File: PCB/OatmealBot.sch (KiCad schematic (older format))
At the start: 23 parts, among them J1 TerminalBlock_5pin_3.5mm, J10 ServoHeader3, J2 RPi_GPIO, J3 TerminalBlock_5pin_3.5mm, J4 ServoHeader1, J5 Motor 3, J6 Motor 4, J7 ServoHeader2, J8 Motor 1, J9 Motor 2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

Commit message: Added second high power connector
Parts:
- added P2, P3: CONN_01X02, symbol CONN_01X02
- added Q1: STP55NF06L, symbol Q_NMOS_GDS
- added R5: 10K, symbol R
- gave numbers to parts that had none: 2
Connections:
- net labels added: HighPower2
- wire segments 148 -> 161
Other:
- note removed: "Add terminal block for headlight"
- moved on the sheet: Q2, R6
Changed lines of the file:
@@
 	6000 4550 5950 4550
 $Comp
-L Q_NMOS_GDS Q?
+L Q_NMOS_GDS Q2
 U 1 1 5B37B0AF
-P 4800 5700
-F 0 "Q?" H 5100 5750 50  0000 R CNN
-F 1 "STP55NF06L" H 5450 5650 50  0000 R CNN
-F 2 "" H 5000 5800 50  0000 C CNN
-F 3 "" H 4800 5700 50  0000 C CNN
-	1    4800 5700
+P 4800 6650
+F 0 "Q2" H 4750 6500 50  0000 R CNN
+F 1 "STP55NF06L" V 5000 6850 50  0000 R CNN
+F 2 "" H 5000 6750 50  0000 C CNN
+F 3 "" H 4800 6650 50  0000 C CNN
+	1    4800 6650
 	1    0    0    -1
 $EndComp
 $Comp
-L GND #PWR?
+L GND #PWR026
 U 1 1 5B37B1D3
-P 4900 6100
-F 0 "#PWR?" H 4900 5850 50  0001 C CNN
-F 1 "GND" H 4900 5950 50  0000 C CNN
-F 2 "" H 4900 6100 50  0000 C CNN
-F 3 "" H 4900 6100 50  0000 C CNN
-	1    4900 6100
+P 4900 7050
+F 0 "#PWR026" H 4900 6800 50  0001 C CNN
+F 1 "GND" H 4900 6900 50  0000 C CNN
+F 2 "" H 4900 7050 50  0000 C CNN
+F 3 "" H 4900 7050 50  0000 C CNN
+	1    4900 7050
 	1    0    0    -1
 $EndComp
 $Comp
-L R R?
+L R R6
 U 1 1 5B37B2B8
-P 4350 5850
-F 0 "R?" V 4430 5850 50  0000 C CNN
-F 1 "10K" V 4350 5850 50  0000 C CNN
-F 2 "" V 4280 5850 50  0000 C CNN
-F 3 "" H 4350 5850 50  0000 C CNN
-	1    4350 5850
+P 4350 6800
+F 0 "R6" V 4430 6800 50  0000 C CNN
+F 1 "10K" V 4350 6800 50  0000 C CNN
+F 2 "" V 4280 6800 50  0000 C CNN
+F 3 "" H 4350 6800 50  0000 C CNN
+	1    4350 6800
 	1    0    0    -1
 $EndComp
 Wire Wire Line
-	4900 5900 4900 6100
+	4900 6850 4900 7050
 Wire Wire Line
-	4150 5700 4600 5700
+	4150 6650 4600 6650
 Wire Wire Line
-	4350 6000 4900 6000
-Connection ~ 4900 6000
+	4350 6950 5200 6950
+Connection ~ 4900 6950
 Text GLabel 5850 2950 0    60   Output ~ 0
 Headlight
 Wire Wire Line
 	6000 2950 5850 2950
-Text GLabel 4150 5700 0    60   Input ~ 0
+Text GLabel 4150 6650 0    60   Input ~ 0
 Headlight
-Connection ~ 4350 5700
-Text Notes 4400 5400 0    60   Italic 0
-Add terminal block for headlight
+Connection ~ 4350 6650
+$Comp
+L CONN_01X02 P3
+U 1 1 5B386F16
+P 5400 6650
+F 0 "P3" H 5400 6800 50  0000 C CNN
+F 1 "CONN_01X02" V 5500 6650 50  0000 C CNN
+F 2 "" H 5400 6650 50  0000 C CNN
+F 3 "" H 5400 6650 50  0000 C CNN
+	1    5400 6650
+	1    0    0    1
+$EndComp
+Wire Wire Line
+	5200 6600 5200 6450
+Wire Wire Line
+	5200 6450 4900 6450
+Wire Wire Line
+	5200 6950 5200 6700
+$Comp
+L Q_NMOS_GDS Q1
+U 1 1 5B3874E0
+P 4750 5750
+F 0 "Q1" H 4700 5600 50  0000 R CNN
+F 1 "STP55NF06L" V 4950 5950 50  0000 R CNN
+F 2 "" H 4950 5850 50  0000 C CNN
+F 3 "" H 4750 5750 50  0000 C CNN
+	1    4750 5750
+	1    0    0    -1
+$EndComp
+$Comp
+L CONN_01X02 P2
+U 1 1 5B387549
+P 5350 5750
+F 0 "P2" H 5350 5900 50  0000 C CNN
+F 1 "CONN_01X02" V 5450 5750 50  0000 C CNN
+F 2 "" H 5350 5750 50  0000 C CNN
+F 3 "" H 5350 5750 50  0000 C CNN
+	1    5350 5750
+	1    0    0    1
+$EndComp
+$Comp
+L GND #PWR027
+U 1 1 5B3875B5
+P 4850 6150
+F 0 "#PWR027" H 4850 5900 50  0001 C CNN
+F 1 "GND" H 4850 6000 50  0000 C CNN
+F 2 "" H 4850 6150 50  0000 C CNN
+F 3 "" H 4850 6150 50  0000 C CNN
+	1    4850 6150
+	1    0    0    -1
+$EndComp
+$Comp
+L R R5
+U 1 1 5B38760E
+P 4350 5900
+F 0 "R5" V 4430 5900 50  0000 C CNN
+F 1 "10K" V 4350 5900 50  0000 C CNN
+F 2 "" V 4280 5900 50  0000 C CNN
+F 3 "" H 4350 5900 50  0000 C CNN
+	1    4350 5900
+	1    0    0    -1
+$EndComp
+Wire Wire Line
+	4850 6150 4850 5950
+Wire Wire Line
+	4350 6050 5150 6050
+Connection ~ 4850 6050
+Wire Wire Line
+	5150 6050 5150 5800
+Wire Wire Line
+	5150 5700 5150 5550
+Wire Wire Line
+	5150 5550 4850 5550
+Wire Wire Line
+	4150 5750 4550 5750
+Text GLabel 4150 5750 0    60   Input ~ 0
+HighPower2
+Text GLabel 5850 3250 0    60   Output ~ 0
+HighPower2
+Wire Wire Line
+	6000 3250 5850 3250
+Connection ~ 4350 5750
+Text GLabel 5350 3650 0    60   Input ~ 0
++3.3V
+Wire Wire Line
+	6000 3450 5450 3450
+Wire Wire Line
+	5450 3450 5450 3650
+Wire Wire Line
+	5450 3650 5350 3650
 $EndSCHEMATC

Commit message: Fixed some of the 3D models. SPI_OLED and the Pololu power connector still aren't lined up properly though.
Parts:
- U2: footprint (none) -> Socket_Strips:Socket_Strip_Straight_1x07_Pitch2.54mm
- U3: footprint (none) -> Pin_Headers:Pin_Header_Angled_1x06_Pitch2.54mm
- U4: footprint (none) -> Socket_Strips:Socket_Strip_Straight_1x05_Pitch2.54mm
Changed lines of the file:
@@
 F 0 "U4" H 10250 1300 60  0000 C CNN
 F 1 "PololuD24V22F" H 10150 700 60  0000 C CNN
-F 2 "" H 9950 1100 60  0001 C CNN
+F 2 "Socket_Strips:Socket_Strip_Straight_1x05_Pitch2.54mm" H 9950 1100 60  0001 C CNN
 F 3 "" H 9950 1100 60  0001 C CNN
 	1    10100 1000
@@
 F 0 "U3" H 9850 5200 60  0000 C CNN
 F 1 "FTDI-Cable" V 10050 5550 60  0000 C CNN
-F 2 "" H 9700 5500 60  0001 C CNN
+F 2 "Pin_Headers:Pin_Header_Angled_1x06_Pitch2.54mm" H 9700 5500 60  0001 C CNN
 F 3 "" H 9700 5500 60  0001 C CNN
 	1    9700 5600
@@
 F 0 "U2" V 7300 5650 60  0000 C CNN
 F 1 "SPI_OLED" H 6900 5450 60  0000 C CNN
-F 2 "" H 6800 5750 60  0001 C CNN
+F 2 "Socket_Strips:Socket_Strip_Straight_1x07_Pitch2.54mm" H 6800 5750 60  0001 C CNN
 F 3 "" H 6800 5750 60  0001 C CNN
 	1    6900 5750

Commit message: Updated to KiCad 4.0.7 (which lost the 3D models I had just gotten working) Assigned more footprints.
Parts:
- D1, D2: footprint (none) -> LEDs:LED_D5.0mm; symbol LED -> LED-RESCUE-OatmealBot
- J10, J4, J7: footprint (none) -> Pin_Headers:Pin_Header_Straight_1x03_Pitch2.54mm
- P1: footprint (none) -> Wire_Pads:SolderWirePad_2x_2mmDrill
- Q1, Q2: footprint (none) -> TO_SOT_Packages_THT:TO-220-3_Vertical
- R1, R2, R3, R4, R5, R6: footprint (none) -> Resistors_SMD:R_0805
- U1: footprint (none) -> SMD_Packages:SSOP-20
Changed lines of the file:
@@
 EESchema Schematic File Version 2
+LIBS:OatmealBot-rescue
 LIBS:power
 LIBS:device
@@
 F 0 "U1" H 3750 2950 60  0000 C CNN
 F 1 "74LVC245A" H 3750 3050 60  0000 C CNN
-F 2 "" H 3750 3500 60  0001 C CNN
+F 2 "SMD_Packages:SSOP-20" H 3750 3500 60  0001 C CNN
 F 3 "" H 3750 3500 60  0001 C CNN
 	1    3750 3500
@@
 F 0 "R2" V 8830 3350 50  0000 C CNN
 F 1 "330" V 8750 3350 50  0000 C CNN
-F 2 "" V 8680 3350 50  0000 C CNN
+F 2 "Resistors_SMD:R_0805" V 8680 3350 50  0000 C CNN
 F 3 "" H 8750 3350 50  0000 C CNN
 	1    8750 3350
@@
 F 0 "R1" V 5780 3350 50  0000 C CNN
 F 1 "330" V 5700 3350 50  0000 C CNN
-F 2 "" V 5630 3350 50  0000 C CNN
+F 2 "Resistors_SMD:R_0805" V 5630 3350 50  0000 C CNN
 F 3 "" H 5700 3350 50  0000 C CNN
 	1    5700 3350
@@
 $EndComp
 $Comp
-L LED D2
+L LED-RESCUE-OatmealBot D2
 U 1 1 5B24C2BD
 P 9200 3350
 F 0 "D2" H 9200 3450 50  0000 C CNN
 F 1 "LED" H 9200 3250 50  0000 C CNN
-F 2 "" H 9200 3350 50  0000 C CNN
+F 2 "LEDs:LED_D5.0mm" H 9200 3350 50  0000 C CNN
 F 3 "" H 9200 3350 50  0000 C CNN
 	1    9200 3350
@@
 $EndComp
 $Comp
-L LED D1
+L LED-RESCUE-OatmealBot D1
 U 1 1 5B24C3DB
 P 5250 3350
 F 0 "D1" H 5250 3450 50  0000 C CNN
 F 1 "LED" H 5250 3250 50  0000 C CNN
-F 2 "" H 5250 3350 50  0000 C CNN
+F 2 "LEDs:LED_D5.0mm" H 5250 3350 50  0000 C CNN
 F 3 "" H 5250 3350 50  0000 C CNN
 	1    5250 3350
@@
 F 0 "J4" V 1600 7200 60  0000 C CNN
 F 1 "ServoHeader1" H 1250 7000 60  0000 C CNN
-F 2 "" H 1200 7350 60  0001 C CNN
+F 2 "Pin_Headers:Pin_Header_Straight_1x03_Pitch2.54mm" H 1200 7350 60  0001 C CNN
 F 3 "" H 1200 7350 60  0001 C CNN
 	1    1250 7350
@@
 F 0 "J7" V 2450 7200 60  0000 C CNN
 F 1 "ServoHeader2" H 2100 7000 60  0000 C CNN
-F 2 "" H 2050 7350 60  0001 C CNN
+F 2 "Pin_Headers:Pin_Header_Straight_1x03_Pitch2.54mm" H 2050 7350 60  0001 C CNN
 F 3 "" H 2050 7350 60  0001 C CNN
 	1    2100 7350
@@
 F 0 "J10" V 3300 7200 60  0000 C CNN
 F 1 "ServoHeader3" H 2950 7000 60  0000 C CNN
-F 2 "" H 2900 7350 60  0001 C CNN
+F 2 "Pin_Headers:Pin_Header_Straight_1x03_Pitch2.54mm" H 2900 7350 60  0001 C CNN
 F 3 "" H 2900 7350 60  0001 C CNN
 	1    2950 7350
@@
 F 0 "P1" H 10000 1750 50  0000 C CNN
 F 1 "Motor Hat Power" H 10200 1450 50  0000 C CNN
-F 2 "" H 10000 1600 50  0000 C CNN
+F 2 "Wire_Pads:SolderWirePad_2x_2mmDrill" H 10000 1600 50  0000 C CNN
 F 3 "" H 10000 1600 50  0000 C CNN
 	1    10000 1600
@@
 F 0 "R3" V 10630 5650 50  0000 C CNN
 F 1 "R" V 10550 5650 50  0000 C CNN
-F 2 "" V 10480 5650 50  0000 C CNN
+F 2 "Resistors_SMD:R_0805" V 10480 5650 50  0000 C CNN
 F 3 "" H 10550 5650 50  0000 C CNN
 	1    10550 5650
@@
 F 0 "R4" V 10630 6150 50  0000 C CNN
 F 1 "R" V 10550 6150 50  0000 C CNN
-F 2 "" V 10480 6150 50  0000 C CNN
+F 2 "Resistors_SMD:R_0805" V 10480 6150 50  0000 C CNN
 F 3 "" H 10550 6150 50  0000 C CNN
 	1    10550 6150
@@
 F 0 "Q2" H 4750 6500 50  0000 R CNN
 F 1 "STP55NF06L" V 5000 6850 50  0000 R CNN
-F 2 "" H 5000 6750 50  0000 C CNN
+F 2 "TO_SOT_Packages_THT:TO-220-3_Vertical" H 5000 6750 50  0000 C CNN
 F 3 "" H 4800 6650 50  0000 C CNN
 	1    4800 6650
@@
 F 0 "R6" V 4430 6800 50  0000 C CNN
 F 1 "10K" V 4350 6800 50  0000 C CNN
-F 2 "" V 4280 6800 50  0000 C CNN
+F 2 "Resistors_SMD:R_0805" V 4280 6800 50  0000 C CNN
 F 3 "" H 4350 6800 50  0000 C CNN
 	1    4350 6800
@@
 F 0 "Q1" H 4700 5600 50  0000 R CNN
 F 1 "STP55NF06L" V 4950 5950 50  0000 R CNN
-F 2 "" H 4950 5850 50  0000 C CNN
+F 2 "TO_SOT_Packages_THT:TO-220-3_Vertical" H 4950 5850 50  0000 C CNN
 F 3 "" H 4750 5750 50  0000 C CNN
 	1    4750 5750
@@
 F 0 "R5" V 4430 5900 50  0000 C CNN
 F 1 "10K" V 4350 5900 50  0000 C CNN
-F 2 "" V 4280 5900 50  0000 C CNN
+F 2 "Resistors_SMD:R_0805" V 4280 5900 50  0000 C CNN
 F 3 "" H 4350 5900 50  0000 C CNN
 	1    4350 5900

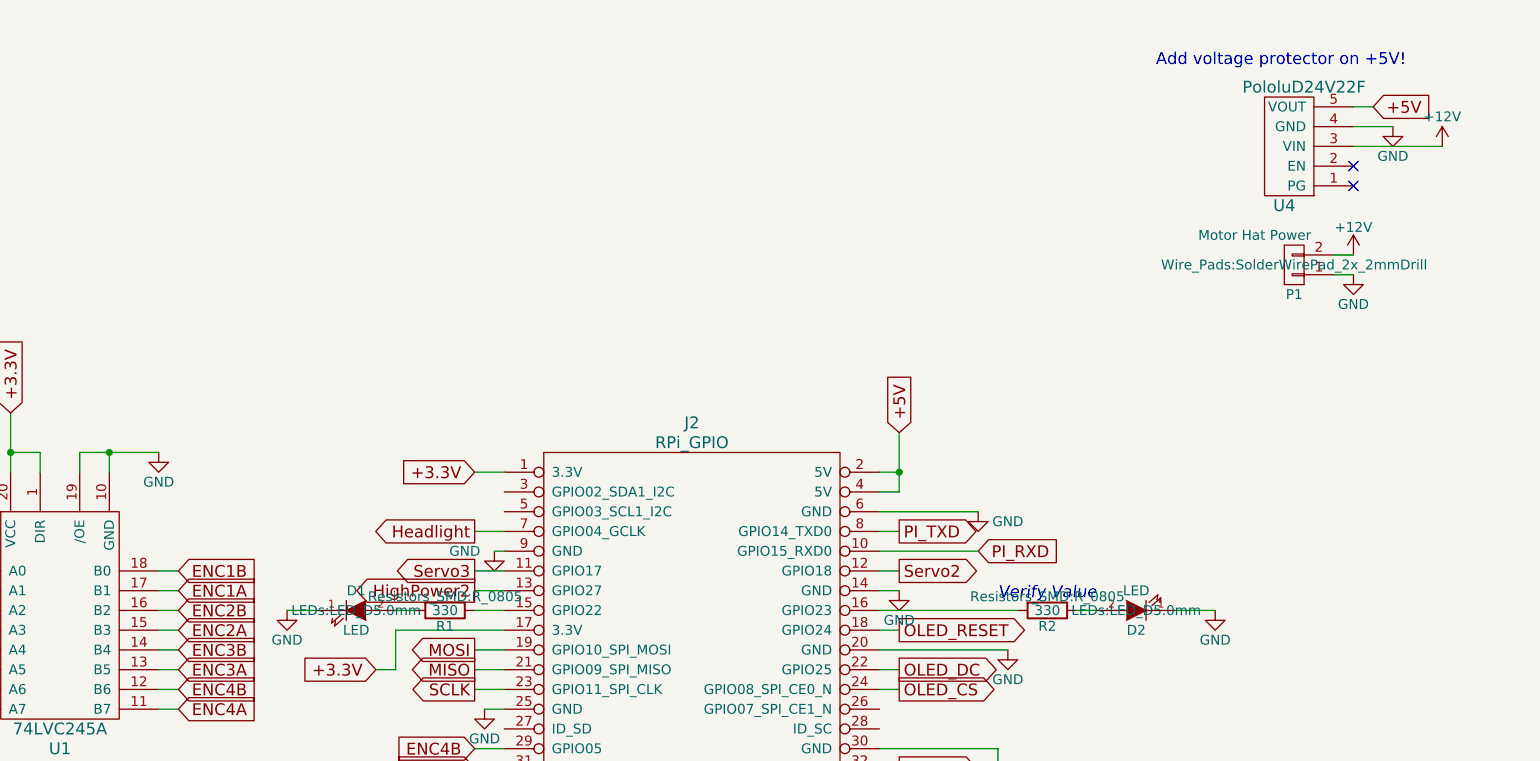
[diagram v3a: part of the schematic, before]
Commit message: Created proper footprint for the voltage regulator so it's easier to see how much space it takes up on the board. Changed the board layout to fit the regulator. Fixed some more 3D files
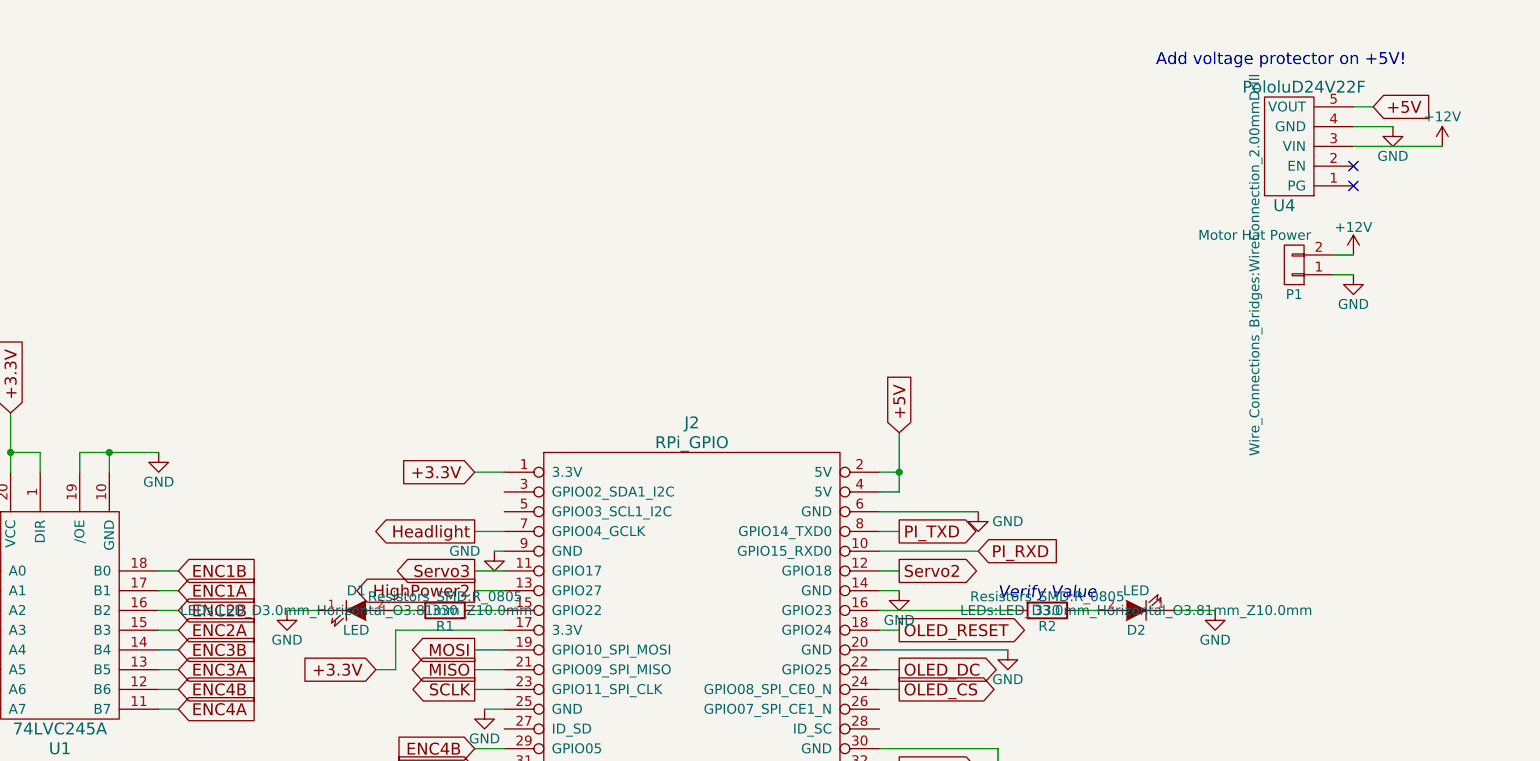
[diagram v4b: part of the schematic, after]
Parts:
- D1, D2: footprint LEDs:LED_D5.0mm -> LEDs:LED_D3.0mm_Horizontal_O3.81mm_Z10.0mm
- P1: footprint Wire_Pads:SolderWirePad_2x_2mmDrill -> Wire_Connections_Bridges:WireConnection_2.00mmDrill
- U4: footprint Socket_Strips:Socket_Strip_Straight_1x05_Pitch2.54mm -> schminktronics:PololuD24V22F
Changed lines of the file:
@@
 F 0 "D2" H 9200 3450 50  0000 C CNN
 F 1 "LED" H 9200 3250 50  0000 C CNN
-F 2 "LEDs:LED_D5.0mm" H 9200 3350 50  0000 C CNN
+F 2 "LEDs:LED_D3.0mm_Horizontal_O3.81mm_Z10.0mm" H 9200 3350 50  0000 C CNN
 F 3 "" H 9200 3350 50  0000 C CNN
 	1    9200 3350
@@
 F 0 "D1" H 5250 3450 50  0000 C CNN
 F 1 "LED" H 5250 3250 50  0000 C CNN
-F 2 "LEDs:LED_D5.0mm" H 5250 3350 50  0000 C CNN
+F 2 "LEDs:LED_D3.0mm_Horizontal_O3.81mm_Z10.0mm" H 5250 3350 50  0000 C CNN
 F 3 "" H 5250 3350 50  0000 C CNN
 	1    5250 3350
@@
 F 0 "U4" H 10250 1300 60  0000 C CNN
 F 1 "PololuD24V22F" H 10150 700 60  0000 C CNN
-F 2 "Socket_Strips:Socket_Strip_Straight_1x05_Pitch2.54mm" H 9950 1100 60  0001 C CNN
+F 2 "schminktronics:PololuD24V22F" H 9950 1100 60  0001 C CNN
 F 3 "" H 9950 1100 60  0001 C CNN
 	1    10100 1000
@@
 F 0 "P1" H 10000 1750 50  0000 C CNN
 F 1 "Motor Hat Power" H 10200 1450 50  0000 C CNN
-F 2 "Wire_Pads:SolderWirePad_2x_2mmDrill" H 10000 1600 50  0000 C CNN
+F 2 "Wire_Connections_Bridges:WireConnection_2.00mmDrill" V 10200 1600 50  0000 C CNN
 F 3 "" H 10000 1600 50  0000 C CNN
 	1    10000 1600
